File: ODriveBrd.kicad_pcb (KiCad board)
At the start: 2 copper layers, 15.7 x 53 mm, 5 parts, among them J1 ODrive, J2 CAN, J3 UART, J4 ENC A, J5 ENC B

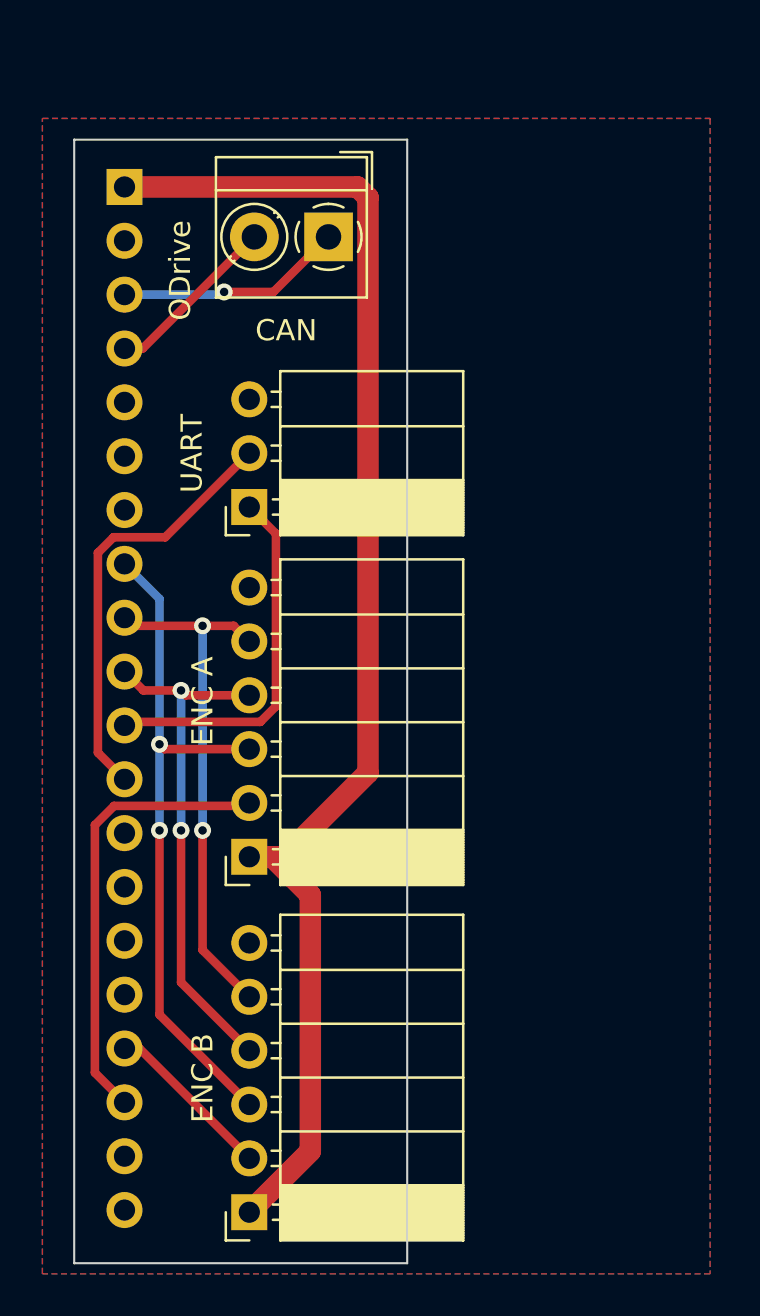
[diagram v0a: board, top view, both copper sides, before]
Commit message: Updated ODrive adapter with isolated serial.
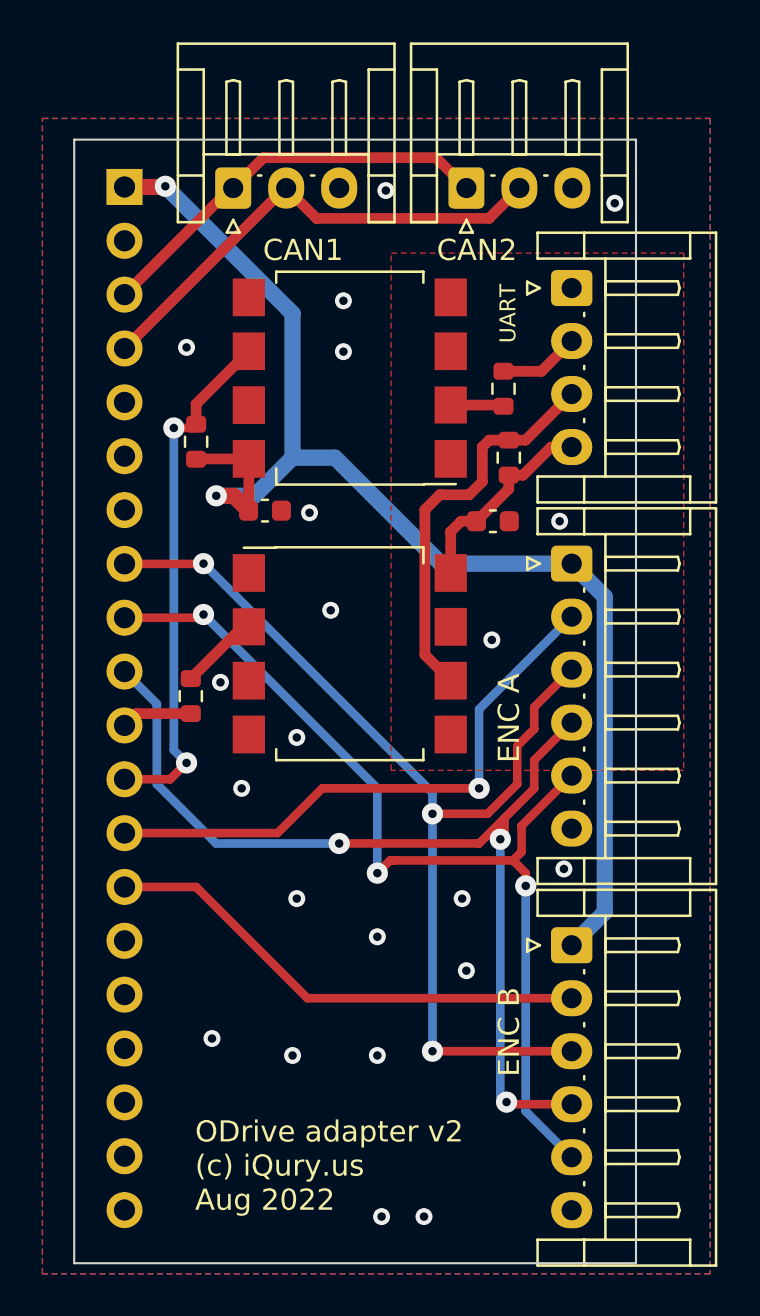
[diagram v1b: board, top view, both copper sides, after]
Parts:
- added C1: 100nF, Capacitor_SMD:C_0603_1608Metric, F.Cu at (133.5, 85.5)
- added C2: 100nF, Capacitor_SMD:C_0603_1608Metric, F.Cu at (144.2, 86.0)
- added J6: Conn_01x04_Male, Connector_JST:JST_EH_S4B-EH_1x04_P2.50mm_Horizontal, F.Cu at (148.0, 75.0)
- added R1: 200, Resistor_SMD:R_0603_1608Metric, F.Cu at (144.8, 79.8)
- added R2: 1k, Resistor_SMD:R_0603_1608Metric, F.Cu at (145.0, 83.0)
- added R3: 1k, Resistor_SMD:R_0603_1608Metric, F.Cu at (130.2, 82.2)
- added R4: 200, Resistor_SMD:R_0603_1608Metric, F.Cu at (130.0, 94.2)
- added U1: 6N137, Package_SO:SSO-8_6.7x9.8mm_P2.54mm_Clearance8mm, F.Cu at (137.5, 92.2)
- added U2: 6N137, Package_SO:SSO-8_6.7x9.8mm_P2.54mm_Clearance8mm, F.Cu at (137.5, 79.2)
- J2: value CAN -> CAN1; footprint TerminalBlock_MetzConnect:TerminalBlock_MetzConnect_Type059_RT06302HBWC_1x02_P3.50mm_Horizontal -> Connector_JST:JST_EH_S3B-EH_1x03_P2.50mm_Horizontal
- J3: value UART -> CAN2; footprint Connector_PinSocket_2.54mm:PinSocket_1x03_P2.54mm_Horizontal -> Connector_JST:JST_EH_S3B-EH_1x03_P2.50mm_Horizontal
- J4, J5: footprint Connector_PinSocket_2.54mm:PinSocket_1x06_P2.54mm_Horizontal -> Connector_JST:JST_EH_S6B-EH_1x06_P2.50mm_Horizontal
- moved J4 20.6 mm to (148.0, 88.0), turned to -90 degrees
- moved J5 19.7 mm to (148.0, 106.0), turned to -90 degrees
- moved J3 18.2 mm to (143.0, 70.3), turned to 0 degrees
- moved J2 5.05 mm to (132.0, 70.3), turned to 0 degrees
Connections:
- net Net-(J1-Pin_1) renamed /3.3V
- J1 pad 11: Net-(J1-Pin_11) -> /TX
- J1 pad 12: Net-(J1-Pin_12) -> /RX
- J1 pad 13: unconnected-(J1-Pin_13) -> Net-(J1-Pin_13)
- J1 pad 14: unconnected-(J1-Pin_14) -> Net-(J1-Pin_14)
- J1 pad 17: Net-(J1-Pin_17) -> unconnected-(J1-Pin_17)
- J1 pad 18: Net-(J1-Pin_18) -> unconnected-(J1-Pin_18)
- J3 pad 1: Net-(J1-Pin_11) -> Net-(J1-Pin_3)
- J3 pad 2: Net-(J1-Pin_12) -> Net-(J1-Pin_4)
- J4 pad 2: Net-(J1-Pin_18) -> Net-(J1-Pin_13)
- J5 pad 2: Net-(J1-Pin_17) -> Net-(J1-Pin_14)
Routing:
- net Net-(J1-Pin_13): track 0.00 -> 27.5 mm, vias 0 -> 1
- net /RX: track 0.00 -> 24.9 mm, vias 0 -> 2
- net Net-(J1-Pin_14): track 0.00 -> 23.3 mm
- net Net-(J1-Pin_10): track 24.7 -> 46.5 mm, vias 2 -> 3
- net Net-(J1-Pin_9): track 24.8 -> 46.3 mm, vias 2 -> 3
- net Net-(J1-Pin_18): track 21.4 -> 0.00 mm
- net Net-(J1-Pin_12): track 20.3 -> 0.00 mm
- net /TX-in: track 0.00 -> 18.7 mm
- net Net-(J1-Pin_11): track 17.4 -> 0.00 mm
- net Net-(J1-Pin_8): track 32.3 -> 48.8 mm, vias 2 -> 3
- net Net-(J1-Pin_4): track 8.30 -> 22.9 mm
- net /3.3V-in: track 0.00 -> 9.70 mm
- net Net-(J1-Pin_3): track 10.8 -> 19.4 mm, vias 1 -> 0
- net Net-(J1-Pin_17): track 8.03 -> 0.00 mm
- net /RX-in: track 0.00 -> 3.81 mm
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- added copper zone on F.Cu, net /GND-in
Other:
- board size 15.7 x 53 mm -> 26.5 x 53 mm
- board text added: "CAN1"
- board text added: "CAN2"
- board text added: "ODrive adapter v2 (c) iQury.us Aug 2022"
- board text added: "VCC"
- board text removed: "(c) iQury.us Feb 2022"
- board text removed: "CAN"
- board text removed: "ODrive"
- board text removed: "ODrive Brk Board V2"

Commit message: Add chip start pin mark.
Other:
- board text added: "*"
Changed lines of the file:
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@@
     (effects (font (size 1 1) (thickness 0.15)) (justify left bottom mirror))
+  )
+  (gr_text "*" (at 130.7 87.9) (layer "F.SilkS")
+    (effects (font (size 1 1) (thickness 0.15)) (justify left bottom))
   )
   (gr_text "CAN2" (at 141.6 73.8) (layer "F.SilkS")
     (effects (font (size 1 1) (thickness 0.15)) (justify left bottom))
   )
+  (gr_text "*" (at 143.2 85.3) (layer "F.SilkS")
+    (effects (font (size 1 1) (thickness 0.15)) (justify left bottom))
+  )

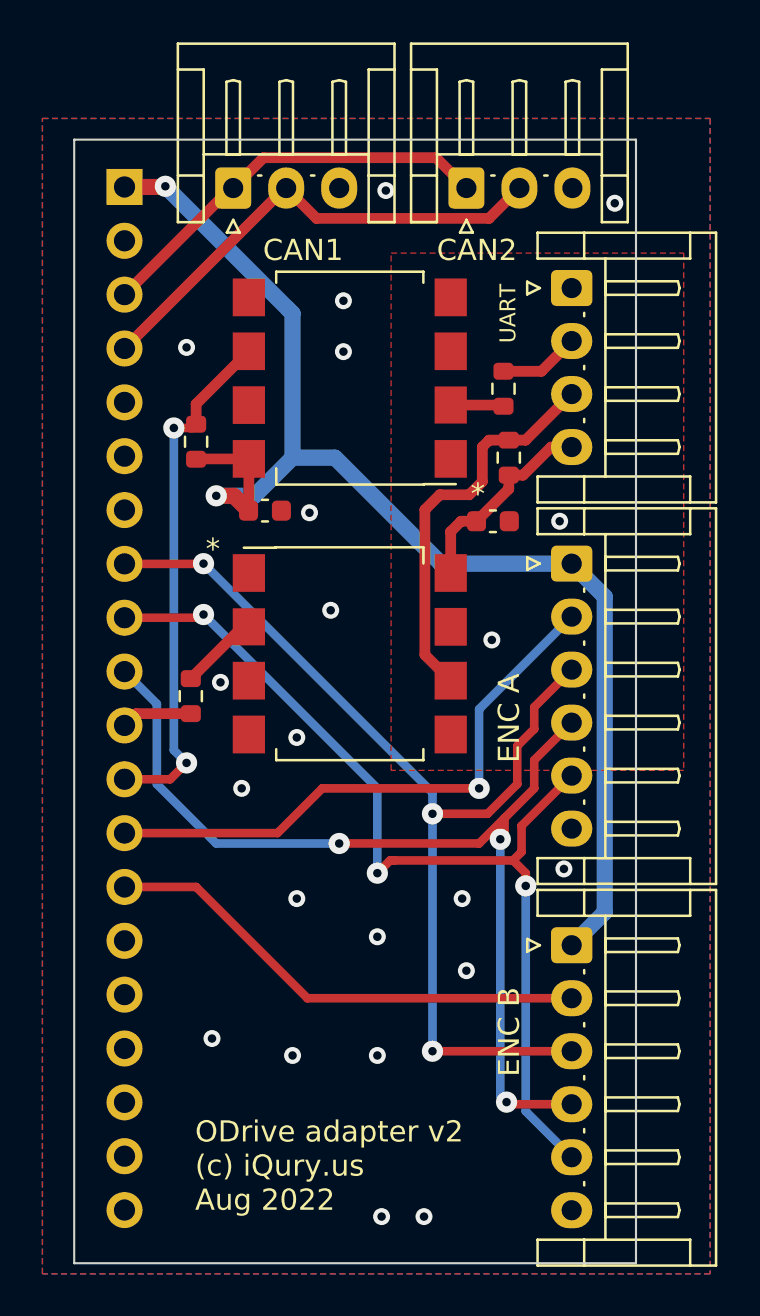
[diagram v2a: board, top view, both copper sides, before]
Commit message: Add inverters to the opto serial adapter.
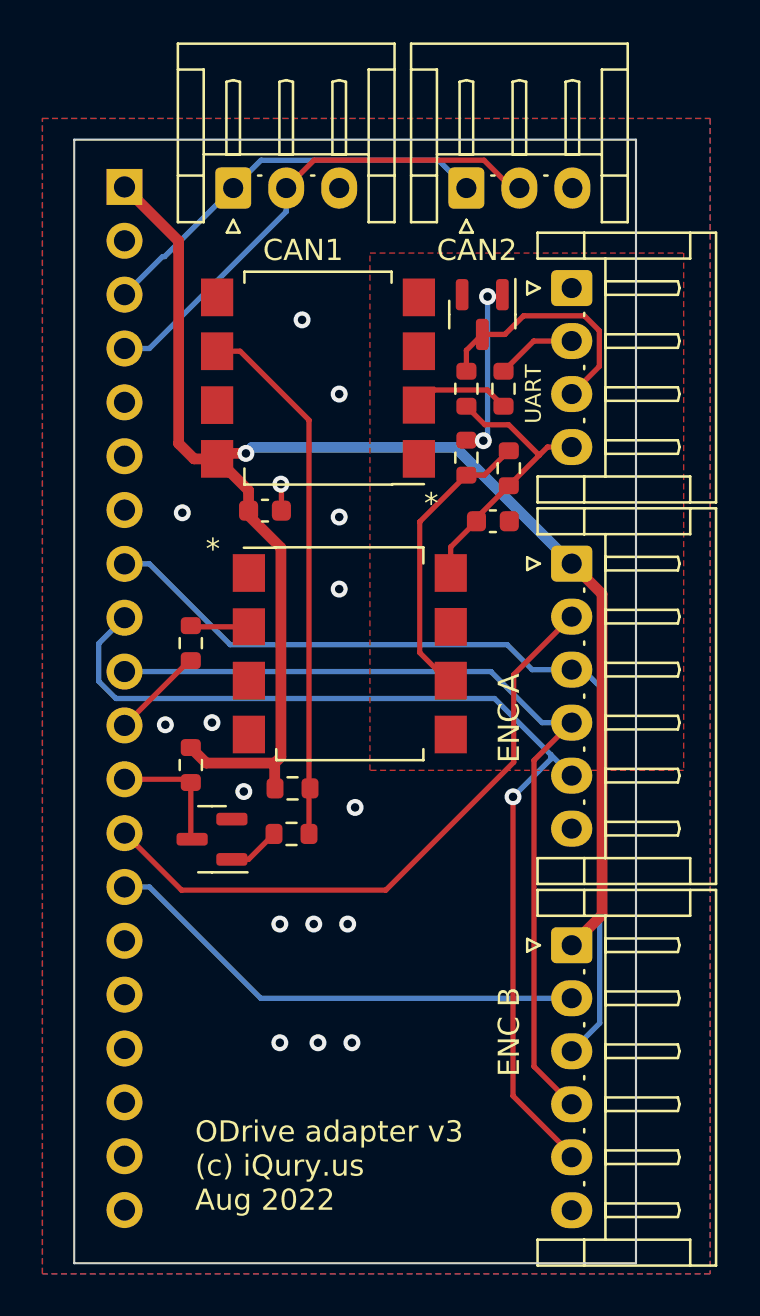
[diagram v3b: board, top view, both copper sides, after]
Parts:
- added Q1: 2N7002, Package_TO_SOT_SMD:SOT-23, F.Cu at (143.8, 76.2)
- added Q2: 2N7002, Package_TO_SOT_SMD:SOT-23, F.Cu at (131.0, 101.0)
- added R5: 1k, Resistor_SMD:R_0603_1608Metric, F.Cu at (143.0, 79.8)
- added R6: 200, Resistor_SMD:R_0603_1608Metric, F.Cu at (143.0, 83.0)
- added R7: 200, Resistor_SMD:R_0603_1608Metric, F.Cu at (134.8, 100.8)
- added R8: 1k, Resistor_SMD:R_0603_1608Metric, F.Cu at (130.0, 97.5)
- J6: value Conn_01x04_Male -> UART
- moved R3 17.0 mm to (134.8, 98.6), turned to 0 degrees
- moved R4 2.50 mm to (130.0, 91.8)
- moved U2 1.50 mm to (136.0, 79.2)
- moved R2 0.50 mm to (145.0, 83.5)
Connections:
- R2 pad 2: /TX-in -> Net-(U1-VO)
- R3 pad 2: /RX -> Net-(U2-VO)
- U1 pad 6: /TX-in -> Net-(U1-VO)
- U2 pad 6: /RX -> Net-(U2-VO)
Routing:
- net Net-(U2-VO): track 0.00 -> 25.2 mm
- net /RX: track 24.9 -> 5.89 mm, vias 2 -> 0
- net Net-(U1-VO): track 0.00 -> 13.8 mm
- net /3.3V: track 62.9 -> 74.9 mm, vias 2 -> 1
- net Net-(Q1-G): track 0.00 -> 8.43 mm, vias 0 -> 2
- net /TX-in: track 18.7 -> 11.8 mm
- net Net-(J1-Pin_8): track 48.8 -> 43.3 mm, vias 3 -> 0
- net Net-(J1-Pin_10): track 46.5 -> 41.6 mm, vias 3 -> 0
- net /3.3V-in: track 9.70 -> 13.4 mm
- net Net-(Q2-G): track 0.00 -> 2.48 mm
- net Net-(J1-Pin_13): track 27.5 -> 30.0 mm, vias 1 -> 0
- net Net-(J1-Pin_9): track 46.3 -> 48.5 mm, vias 3 -> 1
- net Net-(U2-A): track 2.51 -> 4.60 mm
- net GND: track 0.00 -> 1.26 mm, vias 22 -> 16
- net /TX: track 3.36 -> 4.39 mm
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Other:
- board text added: "ODrive adapter v3 (c) iQury.us Aug 2022"
- board text removed: "ODrive adapter v2 (c) iQury.us Aug 2022"
